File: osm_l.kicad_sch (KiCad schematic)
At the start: 1 part, among them U2 OSM-L_Carrier-side

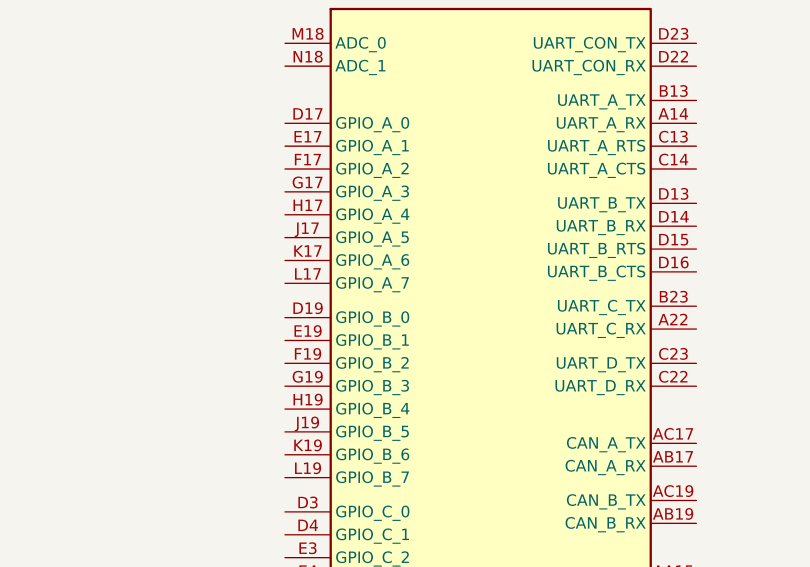
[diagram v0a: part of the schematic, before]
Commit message: [#81876] Add peripheral subsheets
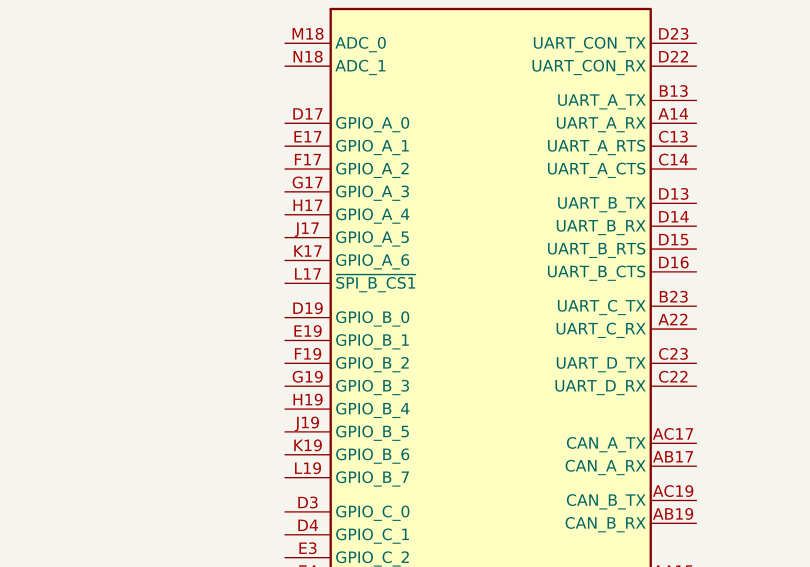
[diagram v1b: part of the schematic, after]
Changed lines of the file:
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@@
 		)
 		(pin "L17"
+			(alternate "~{SPI_B_CS1}")
 		)
 		(pin "AL35"

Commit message: [#81876] Add power section
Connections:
- net OSM_RTC_PWR: now reaches U2.W17 (RTC_PWR)
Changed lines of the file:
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@@
 		(rev "1.0.0")
+	)
+	(wire
+		(pts
+			(xy 166.37 107.95) (xy 170.18 107.95)
+		)
+		(stroke
+			(width 0)
+			(type default)
+		)
 	)
 	(hierarchical_label "OSM_UART_B{UART}"
@@
 		)
 	)
+	(hierarchical_label "OSM_RTC_PWR"
+		(shape input)
+		(at 166.37 107.95 180)
+		(effects
+			(font
+				(size 1.27 1.27)
+			)
+			(justify right)
+		)
+	)
